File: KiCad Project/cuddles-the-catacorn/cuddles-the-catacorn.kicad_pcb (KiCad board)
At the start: 2 copper layers, 61 x 81.1 mm, 43 parts, among them U1 (Pico)

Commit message: First draft
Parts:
- removed D14, D15, D16: LED, LED_SMD:LED_0805_2012Metric_Pad1.15x1.40mm_HandSolder
- removed Down: Down, Button_Switch_SMD:SW_SPST_TL3342
- removed R10, R6, R7, R8, R9: R, Resistor_SMD:R_0805_2012Metric_Pad1.20x1.40mm_HandSolder
- removed Right: Right, Button_Switch_SMD:SW_SPST_TL3342
- added C6: C 0.1uF, Capacitor_SMD:C_0805_2012Metric_Pad1.18x1.45mm_HandSolder, F.Cu at (93.5, 125.5)
- added C7: C 0.1uF, Capacitor_SMD:C_0805_2012Metric_Pad1.18x1.45mm_HandSolder, F.Cu at (97.8, 109.2)
- added C8: C 0.1uF, Capacitor_SMD:C_0805_2012Metric_Pad1.18x1.45mm_HandSolder, F.Cu at (110.3, 108.5)
- added D17: WS2812B, LED_SMD:LED_WS2812B_PLCC4_5.0x5.0mm_P3.2mm, F.Cu at (109.1, 113.3)
- added J2: Conn_01x05, Connector_PinHeader_2.54mm:PinHeader_1x05_P2.54mm_Vertical, F.Cu at (88.9, 108.8)
- added J3: Conn_01x05, Connector_PinHeader_2.54mm:PinHeader_1x05_P2.54mm_Vertical, F.Cu at (117.7, 109.0)
- C1, C2, C5: value C -> C 0.1uF
- C3, C4: value C -> C 0.1uF; moved to B.Cu
- D11, D12: value LED -> WS2812B; footprint LED_SMD:LED_0805_2012Metric_Pad1.15x1.40mm_HandSolder -> LED_SMD:LED_WS2812B_PLCC4_5.0x5.0mm_P3.2mm
- H1, H2: footprint MountingHole:MountingHole_2.2mm_M2 -> MountingHole:MountingHole_2.2mm_M2_Pad
- R1: value R -> R470
- R11: value R -> R470; moved to B.Cu
- R2, R3, R4, R5: value R -> R470; moved to F.Cu
- SW1: renamed from Left; value Left -> C; moved to B.Cu
- SW2: renamed from Up; value Up -> D; moved to B.Cu
- SW3: renamed from B; moved to B.Cu
- SW4: renamed from A; moved to B.Cu
- U1: value (Pico) -> SC0915
- moved SW3 164.3 mm to (77.4, 68.6), turned to 53 degrees
- moved D5 145.6 mm to (87.4, 76.0), turned to 7 degrees
- moved D6 145.2 mm to (99.1, 113.8), turned to 13 degrees
- moved D12 140.4 mm to (88.3, 126.1), turned to 180 degrees
- moved J1 139.6 mm to (96.4, 60.7), turned to 97 degrees
- moved C2 139.4 mm to (73.7, 72.2), turned to 140 degrees
- moved D13 138.4 mm to (101.8, 88.9), turned to 6 degrees
- moved C3 134.4 mm to (87.2, 75.0)
- moved D2 133.5 mm to (76.5, 67.7), turned to -130 degrees
- moved C5 133.1 mm to (112.9, 125.6), turned to -90 degrees
- moved H1 131.0 mm to (72.8, 63.1)
- moved R11 128.3 mm to (77.1, 79.1), turned to -90 degrees
- moved SW4 126.7 mm to (121.8, 63.0), turned to -37 degrees
- moved U1 119.4 mm to (103.6, 103.2), turned to 0 degrees
- moved SW1 118.6 mm to (87.3, 69.7), turned to 7 degrees
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- renumbered Battery to BT1, SAO to J1
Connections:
- BT1 pad MP: GND -> (no net)
- D11 pad 1: GND -> +3V3
- D12 pad 1: GND -> +3V3
- D12 pad 2: Net-(D12-Pad2) -> unconnected-(D12-Pad2)
- D6 pad 2: unconnected-(D6-Pad2) -> Net-(D6-Pad2)
- R2 pad 2: Net-(R1-Pad2) -> Net-(U1-Pad20)
- R3 pad 2: Net-(R1-Pad2) -> Net-(U1-Pad20)
- R4 pad 2: Net-(R1-Pad2) -> Net-(U1-Pad20)
- R5 pad 1: Net-(D11-Pad2) -> Net-(D13-Pad2)
- R5 pad 2: Net-(R1-Pad2) -> Net-(U1-Pad17)
- SW3 pad 1: Net-(SW5-Pad1) -> Net-(U1-Pad25)
- SW4 pad 1: Net-(SW6-Pad1) -> Net-(SW4-Pad1)
- U1 pad 10: unconnected-(U1-Pad10) -> Net-(U1-Pad10)
- U1 pad 11: unconnected-(U1-Pad11) -> Net-(U1-Pad11)
- U1 pad 12: unconnected-(U1-Pad12) -> Net-(U1-Pad12)
- U1 pad 14: unconnected-(U1-Pad14) -> Net-(U1-Pad14)
- U1 pad 15: unconnected-(U1-Pad15) -> Net-(U1-Pad15)
- U1 pad 17: unconnected-(U1-Pad17) -> Net-(U1-Pad17)
- U1 pad 20: Net-(R10-Pad2) -> Net-(U1-Pad20)
- U1 pad 21: Net-(SW6-Pad1) -> unconnected-(U1-Pad21)
- U1 pad 22: Net-(SW5-Pad1) -> unconnected-(U1-Pad22)
- U1 pad 24: Net-(SW3-Pad1) -> Net-(SW4-Pad1)
- U1 pad 25: Net-(SW4-Pad1) -> Net-(U1-Pad25)
- U1 pad 4: unconnected-(U1-Pad4) -> Net-(U1-Pad4)
- U1 pad 5: unconnected-(U1-Pad5) -> Net-(U1-Pad5)
- U1 pad 9: unconnected-(U1-Pad9) -> Net-(U1-Pad9)
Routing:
- net +3V3: track 179.2 -> 0.00 mm, vias 4 -> 0
- net Net-(R1-Pad2): track 87.0 -> 0.00 mm
- net Net-(D1-Pad1): track 55.8 -> 0.00 mm
- net Net-(D2-Pad2): track 52.7 -> 0.00 mm, vias 2 -> 0
- net Net-(SW4-Pad1): track 50.2 -> 0.00 mm, vias 3 -> 0
- net /LED_DATA_1: track 49.2 -> 0.00 mm, vias 1 -> 0
- net Net-(D5-Pad2): track 45.5 -> 0.00 mm, vias 2 -> 0
- net Net-(SW5-Pad1): track 43.3 -> 0.00 mm, vias 1 -> 0
- net Net-(SW6-Pad1): track 35.2 -> 0.00 mm, vias 1 -> 0
- net Net-(SW1-Pad1): track 30.2 -> 0.00 mm, vias 1 -> 0
- net Net-(R10-Pad2): track 27.4 -> 0.00 mm
- net Net-(SW3-Pad1): track 27.2 -> 0.00 mm, vias 3 -> 0
- net Net-(SW2-Pad1): track 22.7 -> 0.00 mm, vias 1 -> 0
- net Net-(D4-Pad2): track 16.1 -> 0.00 mm
- net Net-(D3-Pad2): track 15.5 -> 0.00 mm
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- removed copper zone on B.Cu, net GND
- removed copper zone on F.Cu, net GND
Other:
- board size 61 x 81.1 mm -> 68 x 81.5 mm
- board text added: "Cuddles the Catacorn by @GalaxyAllie and friends"
- board text removed: "+"
- board text removed: "GP16"
- board text removed: "GP17"
- board text removed: "GP18"
- board text removed: "GP19"
- board text removed: "GP20"
- board text removed: "GP21"
- board text removed: "Molly the Mermaid by @GalaxyAllie and friends"

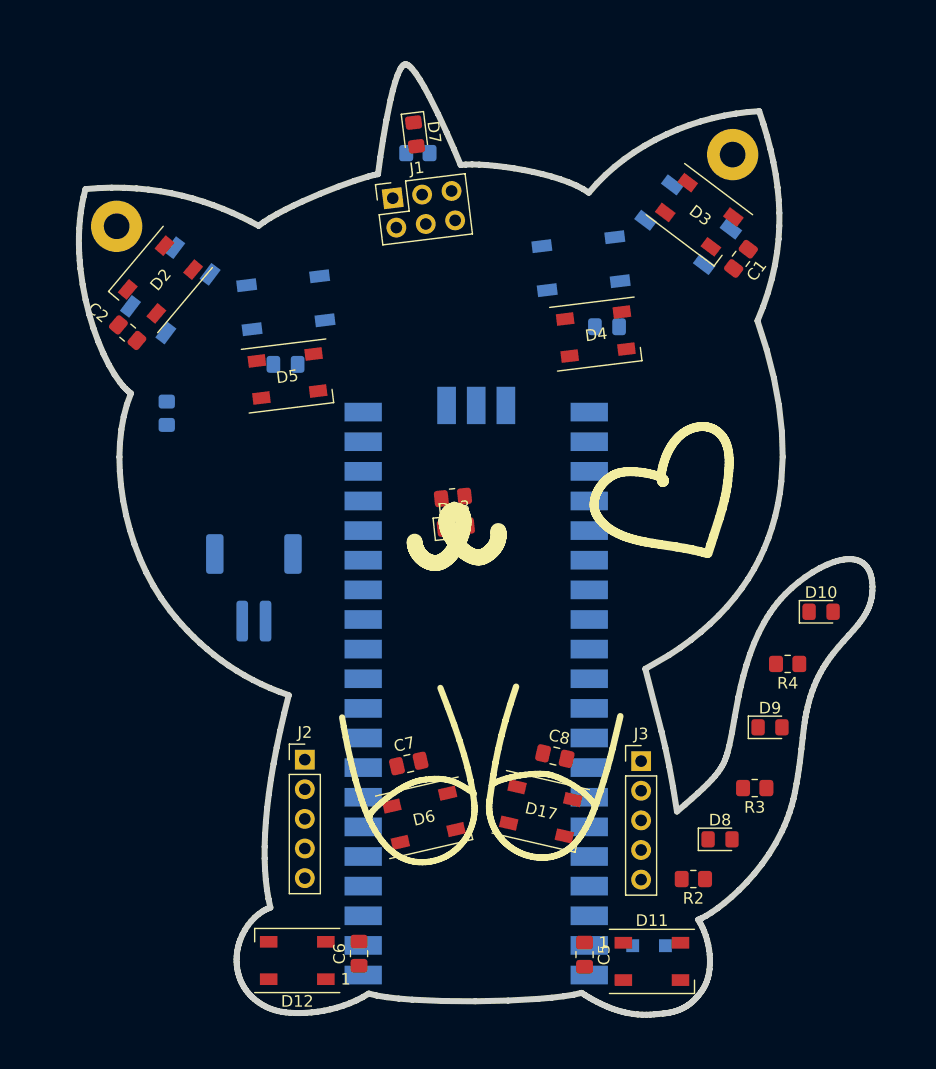
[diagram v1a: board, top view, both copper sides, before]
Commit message: Schematic changes to simplify routing
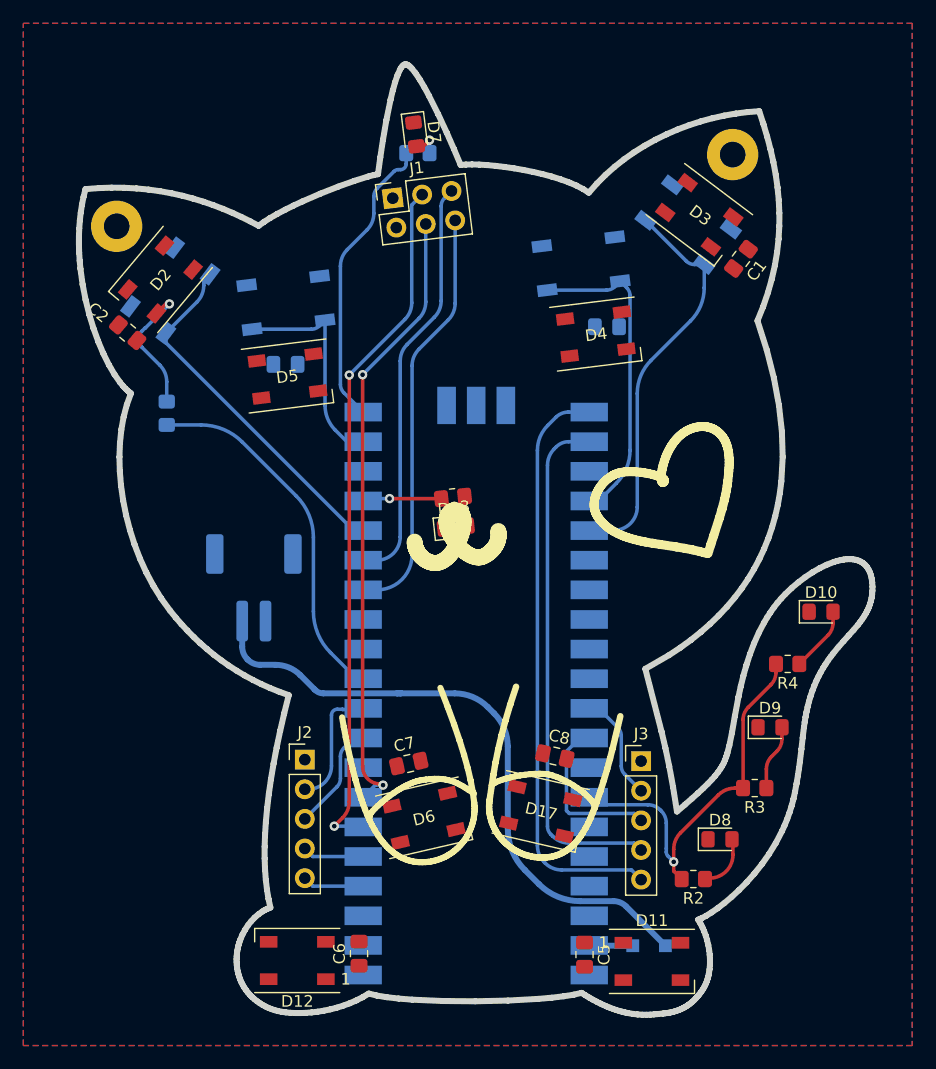
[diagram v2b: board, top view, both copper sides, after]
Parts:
- SW1: value C -> D
- SW2: value D -> C
- turned R11 to 90 degrees
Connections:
- J3 pad 2: Net-(U1-Pad15) -> /GP26
- J3 pad 3: Net-(U1-Pad14) -> /GP27
- J3 pad 4: Net-(U1-Pad12) -> /GP17
- J3 pad 5: Net-(U1-Pad11) -> /GP16
- R2 pad 2: Net-(U1-Pad20) -> /Tail
- R3 pad 2: Net-(U1-Pad20) -> /Tail
- R4 pad 2: Net-(U1-Pad20) -> /Tail
- SW1 pad 1: Net-(SW1-Pad1) -> /GP14
- SW3 pad 1: Net-(U1-Pad25) -> /GP12
- U1 pad 1: /SAO1 -> unconnected-(U1-Pad1)
- U1 pad 11: Net-(U1-Pad11) -> /LED_DATA_1
- U1 pad 12: Net-(U1-Pad12) -> unconnected-(U1-Pad12)
- U1 pad 14: Net-(U1-Pad14) -> /SAO2
- U1 pad 15: Net-(U1-Pad15) -> /SAO1
- U1 pad 16: unconnected-(U1-Pad16) -> /GP12
- U1 pad 19: Net-(R1-Pad2) -> /GP14
- U1 pad 2: /SAO2 -> unconnected-(U1-Pad2)
- U1 pad 20: Net-(U1-Pad20) -> Net-(R1-Pad2)
- U1 pad 21: unconnected-(U1-Pad21) -> /GP16
- U1 pad 22: unconnected-(U1-Pad22) -> /GP17
- U1 pad 24: Net-(SW4-Pad1) -> Net-(SW2-Pad1)
- U1 pad 25: Net-(U1-Pad25) -> Net-(SW4-Pad1)
- U1 pad 26: Net-(SW1-Pad1) -> unconnected-(U1-Pad26)
- U1 pad 27: Net-(SW2-Pad1) -> unconnected-(U1-Pad27)
- U1 pad 29: /LED_DATA_1 -> unconnected-(U1-Pad29)
- U1 pad 31: unconnected-(U1-Pad31) -> /GP26
- U1 pad 32: unconnected-(U1-Pad32) -> /GP27
- U1 pad 34: unconnected-(U1-Pad34) -> /Tail
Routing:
- net /SDA: track 0.00 -> 59.6 mm, vias 0 -> 2
- net +BATT: track 0.00 -> 54.9 mm
- net /SCL: track 0.00 -> 53.4 mm, vias 0 -> 2
- net /GP16: track 0.00 -> 50.6 mm
- net /GP17: track 0.00 -> 44.6 mm
- net /SAO2: track 0.00 -> 35.8 mm
- net /SAO1: track 0.00 -> 35.5 mm
- net Net-(SW4-Pad1): track 0.00 -> 34.5 mm
- net /Tail: track 0.00 -> 34.2 mm, vias 0 -> 1
- net /GP12: track 0.00 -> 33.5 mm
- net /LED_DATA_1: track 0.00 -> 31.3 mm
- net Net-(SW2-Pad1): track 0.00 -> 27.4 mm
- net Net-(R1-Pad2): track 0.00 -> 25.3 mm
- net /GP14: track 0.00 -> 19.0 mm
- net /GP27: track 0.00 -> 14.2 mm
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- added copper zone on B.Cu, net GND
- added copper zone on F.Cu, net GND

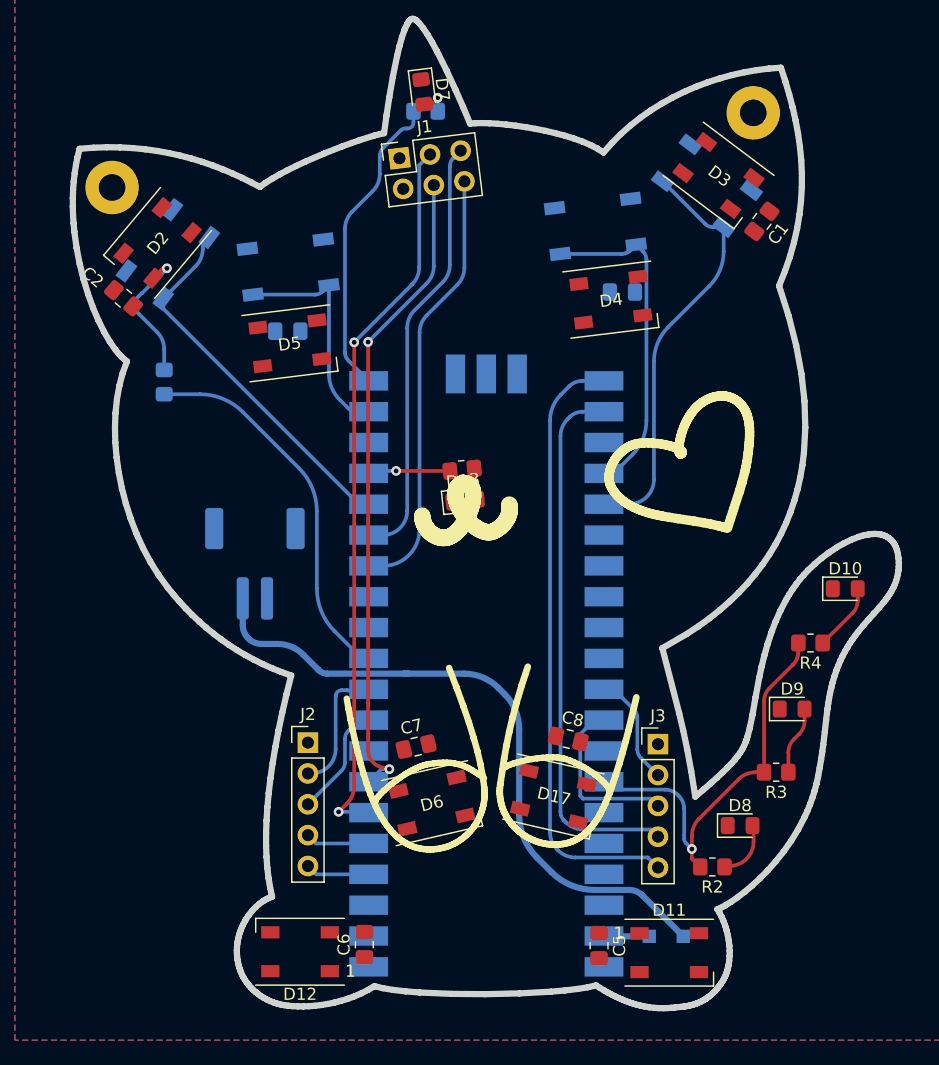
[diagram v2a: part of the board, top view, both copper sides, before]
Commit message: DRC errors cleared
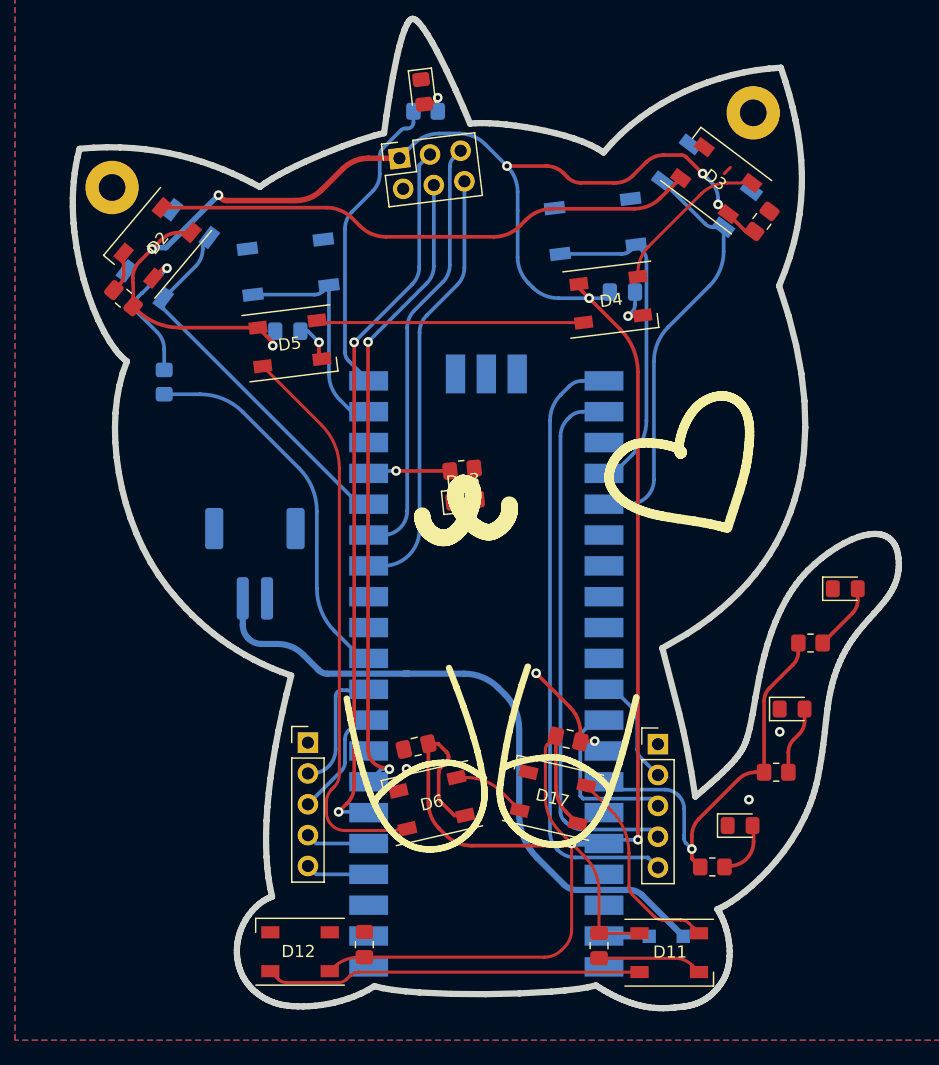
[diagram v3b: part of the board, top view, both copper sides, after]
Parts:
- moved D3 0.46 mm to (122.5, 62.6), turned to 143 degrees
- moved D17 0.12 mm to (109.1, 113.4), turned to 167 degrees
- turned C1 to 53 degrees
- turned C7 to -167 degrees
- turned D6 to -167 degrees
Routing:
- net +3V3: track 0.00 -> 237.3 mm, vias 0 -> 9
- net Net-(D5-Pad2): track 0.00 -> 46.9 mm
- net Net-(D2-Pad2): track 0.00 -> 45.0 mm
- net Net-(D11-Pad2): track 0.00 -> 31.0 mm
- net GND: track 0.00 -> 27.1 mm, vias 0 -> 7
- net Net-(D4-Pad2): track 0.00 -> 22.0 mm
- net Net-(D17-Pad2): track 0.00 -> 17.0 mm
- net Net-(D3-Pad2): track 0.00 -> 13.2 mm
- net Net-(D6-Pad2): track 0.00 -> 6.12 mm
- net (no net): track 0.00 -> 0.72 mm
